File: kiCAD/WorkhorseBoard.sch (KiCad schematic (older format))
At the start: 0 parts

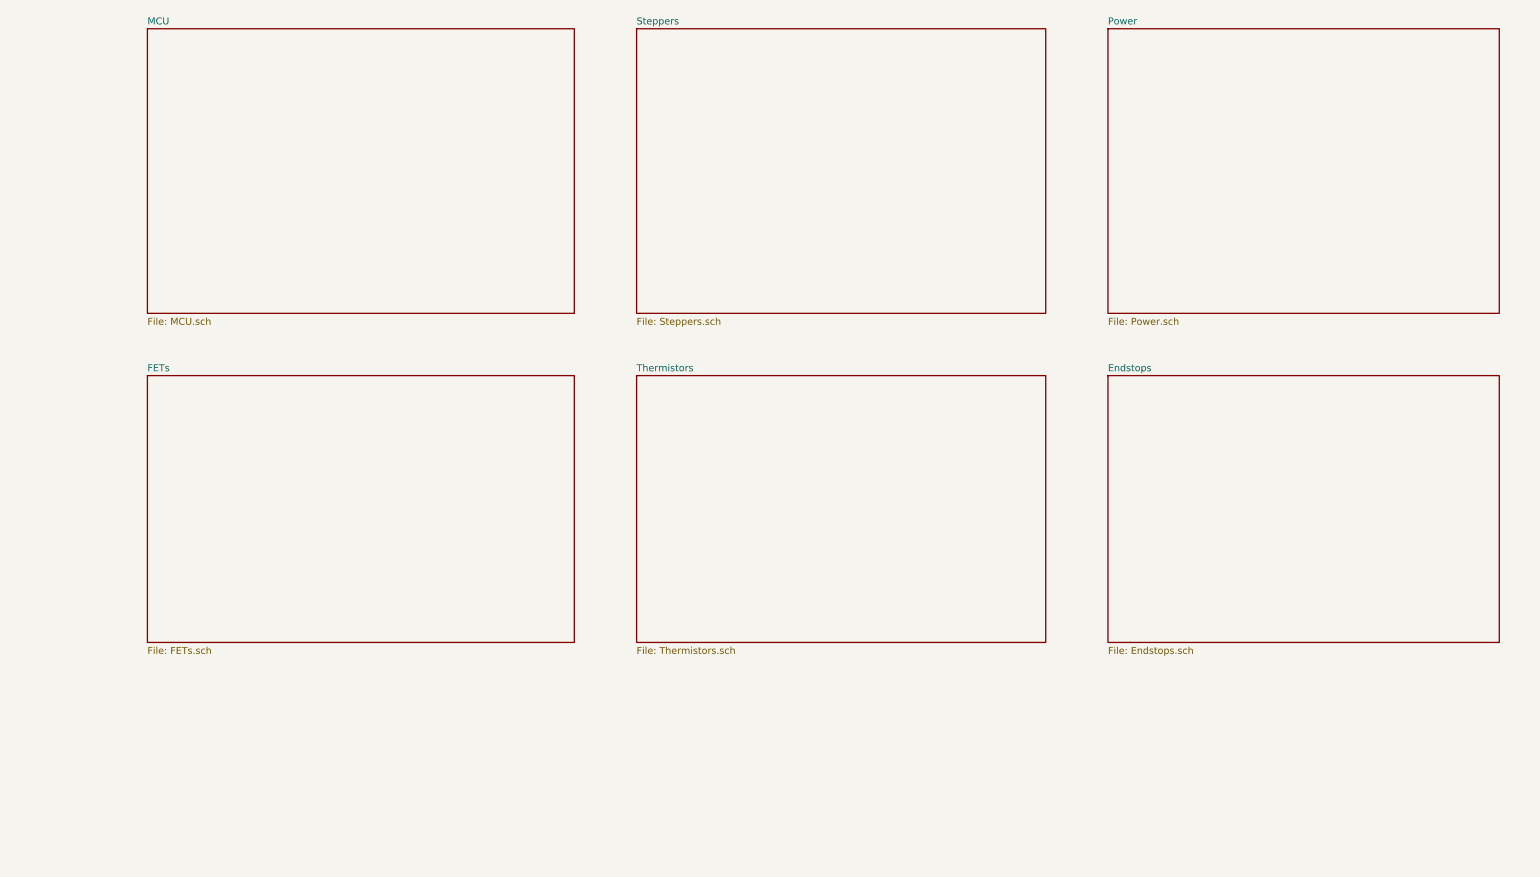
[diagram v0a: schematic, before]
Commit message: Completed Schematic, assigned footprints.
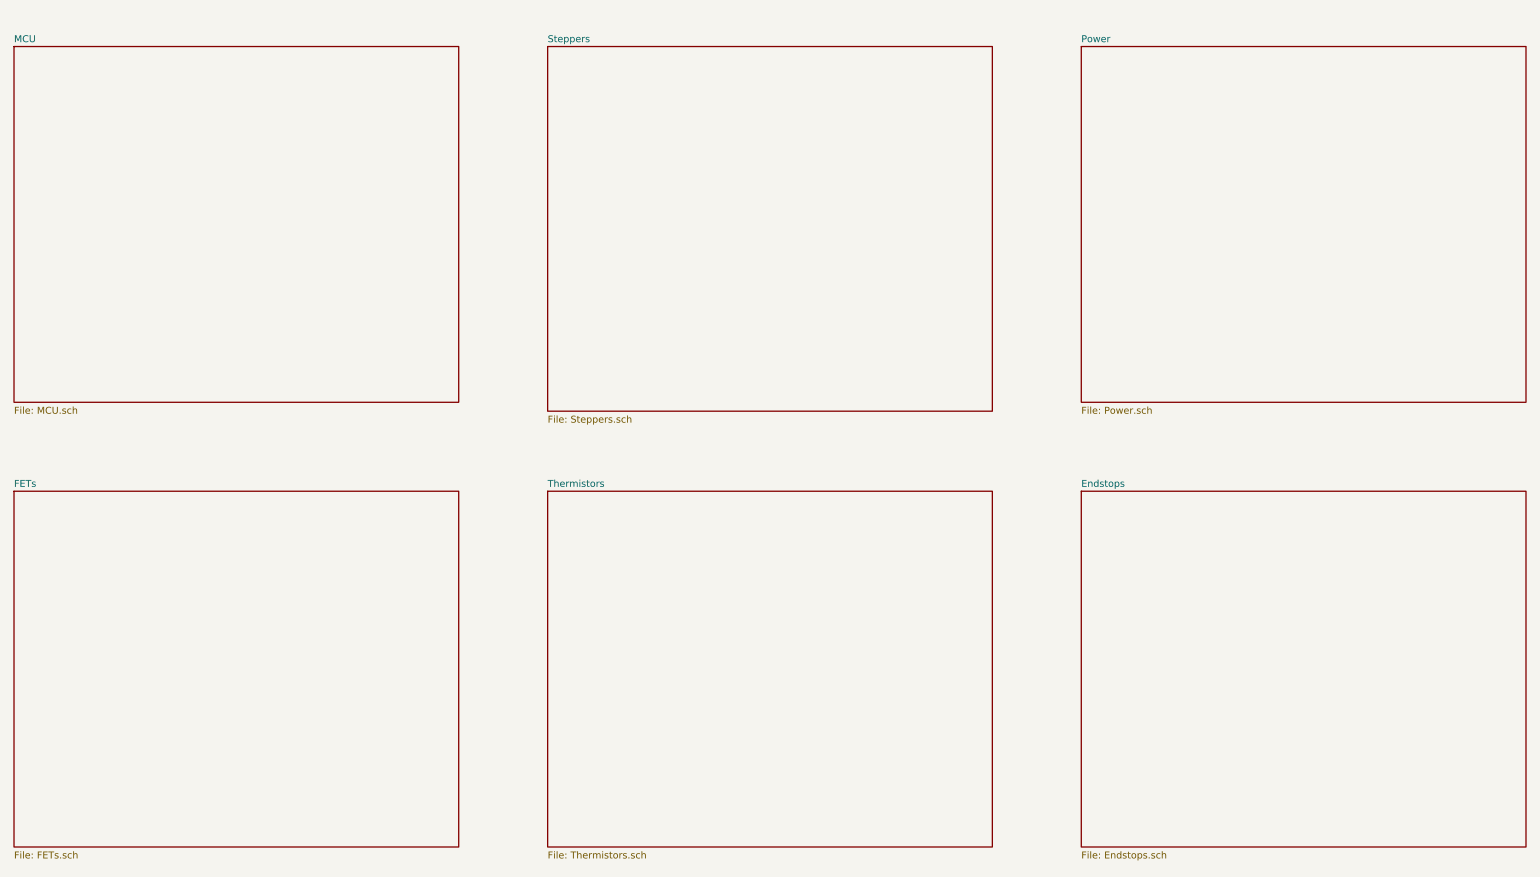
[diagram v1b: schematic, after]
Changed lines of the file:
@@
 $EndDescr
 $Sheet
-S 2250 1400 2400 1600
+S 1500 1500 2500 2000
 U 5FAD93BD
 F0 "MCU" 39
@@
 $EndSheet
 $Sheet
-S 5000 1400 2300 1600
+S 4500 1500 2500 2050
 U 5FAD943D
 F0 "Steppers" 39
@@
 $EndSheet
 $Sheet
-S 7650 1400 2200 1600
+S 7500 1500 2500 2000
 U 5FAD9549
 F0 "Power" 39
@@
 $EndSheet
 $Sheet
-S 2250 3350 2400 1500
+S 1500 4000 2500 2000
 U 5FAD965A
 F0 "FETs" 39
@@
 $EndSheet
 $Sheet
-S 5000 3350 2300 1500
+S 4500 4000 2500 2000
 U 5FAD96B3
 F0 "Thermistors" 39
@@
 $EndSheet
 $Sheet
-S 7650 3350 2200 1500
+S 7500 4000 2500 2000
 U 5FAD9712
 F0 "Endstops" 39
